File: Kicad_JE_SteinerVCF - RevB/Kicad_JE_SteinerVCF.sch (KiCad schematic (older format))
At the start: 49 parts, among them J101 HP, J102 BP, J103 LP, J104 Out, J105 CV, P101 Doepfer_Power_10pin, Q101 BC559, Q102 BC549, Q103 BC549, Q104 BC549

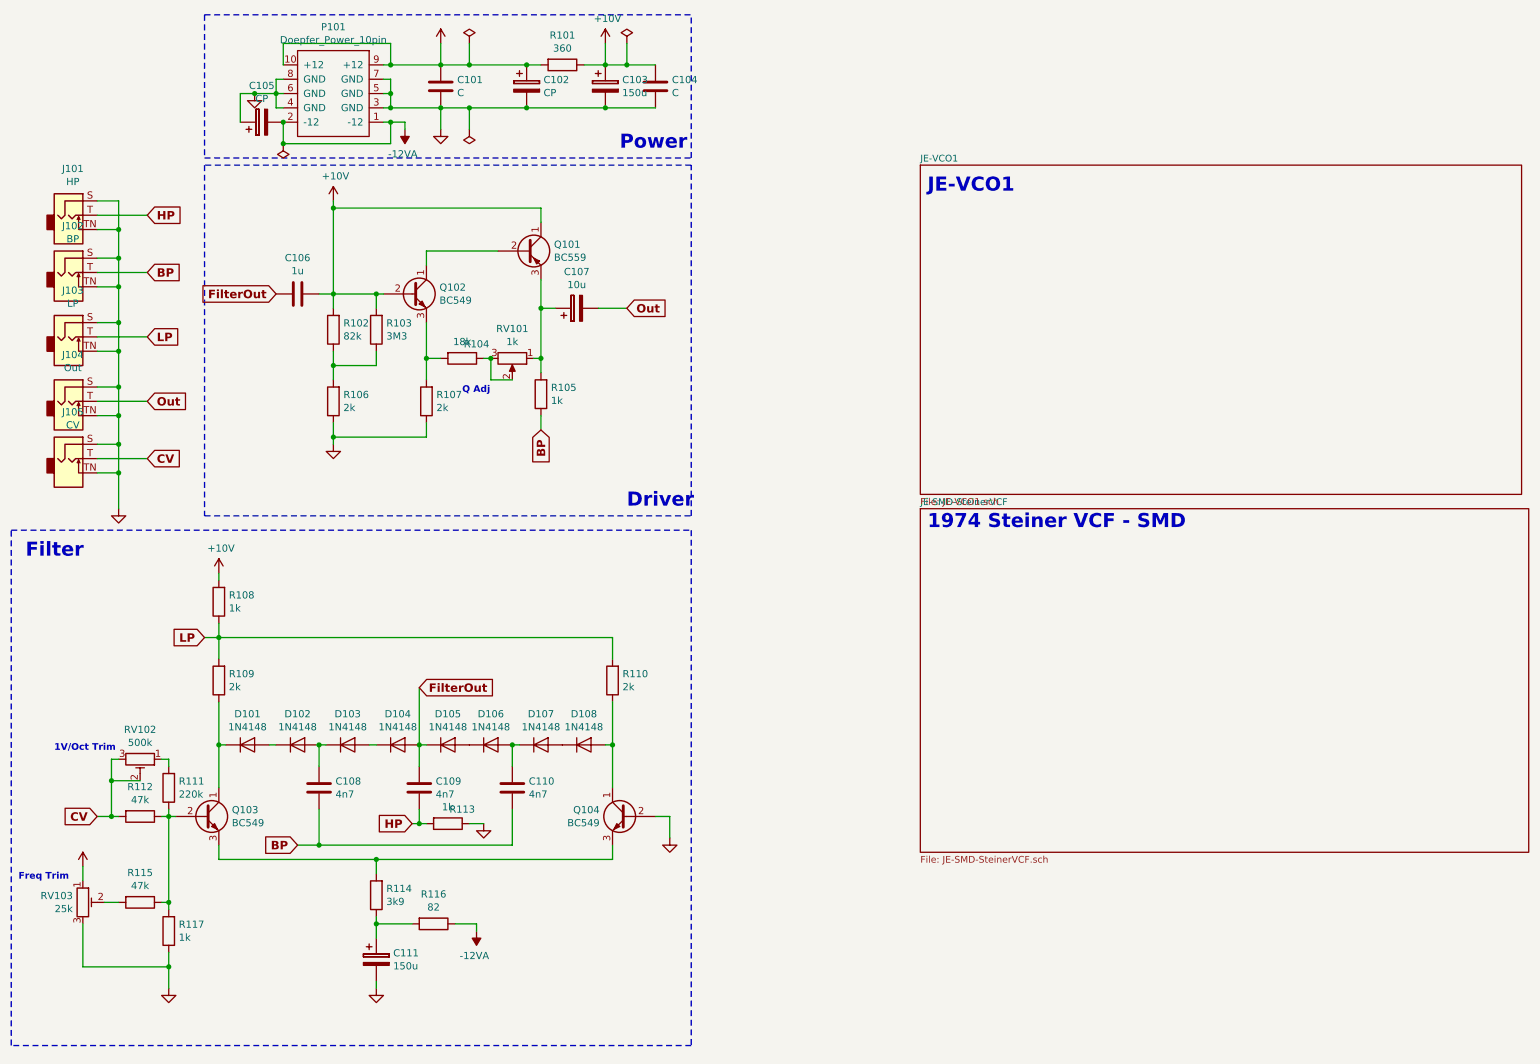
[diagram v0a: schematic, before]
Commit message: VCF Rev B THT + Extra inspiration
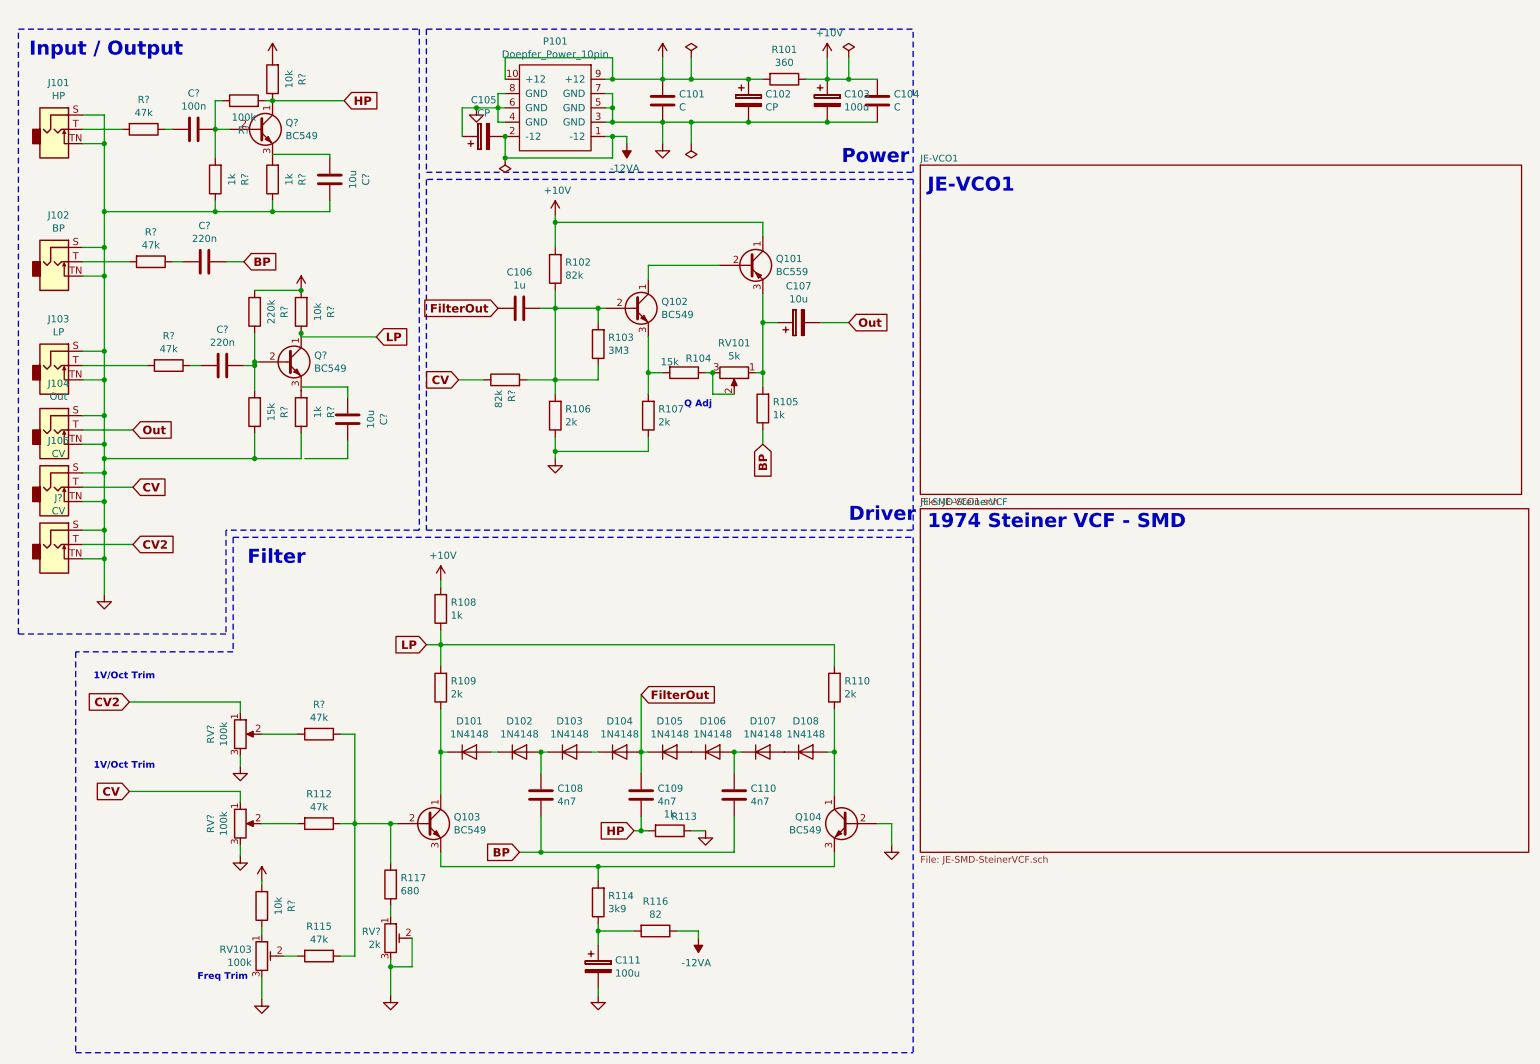
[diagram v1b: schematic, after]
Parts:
- removed R111: 220k, Resistor_THT:R_Axial_DIN0309_L9.0mm_D3.2mm_P12.70mm_Horizontal, symbol Device:R
- removed RV102: 500k, Potentiometer_THT:Potentiometer_Alps_RK09K_Single_Vertical, symbol Device:R_POT_TRIM
- added C? (x2): 220n, Capacitor_THT:C_Rect_L7.0mm_W2.0mm_P5.00mm, symbol Device:C
- added C?: 100n, Capacitor_THT:C_Rect_L7.0mm_W2.0mm_P5.00mm, symbol Device:C
- added C? (x2): 10u, Capacitor_THT:C_Rect_L7.0mm_W2.0mm_P5.00mm, symbol Device:C
- added J?: CV, AJ-Dropbox-Kicad:PJ301SM, symbol Connector:AudioJack2_SwitchT
- added Q? (x2): BC549, Package_TO_SOT_THT:TO-92_Inline, symbol Transistor_BJT:BC549
- added R?: 82k, Resistor_THT:R_Axial_DIN0309_L9.0mm_D3.2mm_P12.70mm_Horizontal, symbol Device:R
- added R? (x3): 10k, Resistor_THT:R_Axial_DIN0309_L9.0mm_D3.2mm_P12.70mm_Horizontal, symbol Device:R
- added R? (x4): 47k, Resistor_THT:R_Axial_DIN0309_L9.0mm_D3.2mm_P12.70mm_Horizontal, symbol Device:R
- added R? (x3): 1k, Resistor_THT:R_Axial_DIN0309_L9.0mm_D3.2mm_P12.70mm_Horizontal, symbol Device:R
- added R?: 220k, Resistor_THT:R_Axial_DIN0309_L9.0mm_D3.2mm_P12.70mm_Horizontal, symbol Device:R
- added R?: 15k, Resistor_THT:R_Axial_DIN0309_L9.0mm_D3.2mm_P12.70mm_Horizontal, symbol Device:R
- added R?: 100k, Resistor_THT:R_Axial_DIN0309_L9.0mm_D3.2mm_P12.70mm_Horizontal, symbol Device:R
- added RV?: 2k, Potentiometer_THT:Potentiometer_Piher_PT-6-V_Vertical, symbol Device:R_POT_TRIM
- added RV? (x2): 100k, Potentiometer_THT:Potentiometer_Alps_RK09K_Single_Vertical, symbol Device:R_POT
- C103, C111: value 150u -> 100u
- R104: value 18k -> 15k
- R117: value 1k -> 680
- RV101: value 1k -> 5k
- RV103: value 25k -> 100k
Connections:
- net +10V: no longer C106.1, Q102.2 (B), R103.2
- net +12VA: now also R?.2, R?.2, R?.2, R?.2; no longer RV103.1
- net BP: now also C?.1; no longer J102.T
- net CV: now also R?.1, RV?.1; no longer R112.2
- net GNDA: now also C?.1, J?.S, J?.TN, R?.1, R?.1, R?.1, R?.1, RV?.2, RV?.3, RV?.3, RV?.3; no longer R117.1
- net HP: now also Q?.1 (C), R?.1, R?.2; no longer J101.T
- net LP: now also Q?.1 (C), R?.1; no longer J103.T
- net at Q103.2 (B), R112.1, R115.1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: now also R?.1
- net at R102.1, R103.1, R106.2: now also C106.1, Q102.2 (B), R103.2, R?.2
- new net: R112.2, RV?.2
- new net: R117.1, RV?.1
- new net: J101.T, R?.2
- new net: J102.T, R?.2
- new net: J103.T, R?.2
- new net: R?.1, RV103.1
- new net: R?.2, RV?.2
- new net: C?.1, Q?.2 (B), R?.1, R?.2 (x2)
- new net: Q?.3 (E), R?.2 (x2)
- new net: C?.2, R?.1 (x3)
- new net CV2: J?.T, RV?.1
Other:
- note added: "Input / Output"
- moved on the sheet: C101, C102, C103, C104, C105, C106, C107, C108, C109, C110, C111, D101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

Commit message: fix reintroduced
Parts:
- added R? (x2): 1k, Resistor_THT:R_Axial_DIN0309_L9.0mm_D3.2mm_P12.70mm_Horizontal, symbol Device:R
- R?: value 1k -> 10k
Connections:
- net HP: now also R?.2; no longer Q?.1 (C), R?.1, R?.2
- net LP: now also R?.2; no longer Q?.1 (C), R?.1
- net at R102.1, R103.1, R106.2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: no longer C106.1, Q102.2 (B), R103.2
- new net: C106.1, Q102.2 (B), R103.2
- new net: Q?.1 (C), R?.1, R?.1, R?.2
- new net: Q?.1 (C), R?.1, R?.1
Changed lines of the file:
@@
 JE-VCO1
 Wire Wire Line
-	4350 2425 4350 2550
-Wire Wire Line
 	4250 2550 4350 2550
-Wire Wire Line
-	4350 2550 4350 3050
 Text GLabel 3675 3050 0    59   Input ~ 12
 CV
@@
 Wire Wire Line
 	3675 3050 3850 3050
-Connection ~ 4350 2550
 Wire Wire Line
 	4350 2550 4650 2550
@@
 Connection ~ 2375 1875
 Wire Wire Line
-	2375 1100 2875 1100
-Wire Wire Line
-	2575 2750 3100 2750
+	2375 1100 2500 1100
+Wire Wire Line
+	2575 2750 2700 2750
 Connection ~ 3200 6150
 Wire Wire Line
@@
 P 1975 1650
 F 0 "R?" V 1768 1650 50  0000 C CNN
-F 1 "1k" V 1859 1650 50  0000 C CNN
+F 1 "10k" V 1859 1650 50  0000 C CNN
 F 2 "Resistor_THT:R_Axial_DIN0309_L9.0mm_D3.2mm_P12.70mm_Horizontal" V 1905 1650 50  0001 C CNN
 F 3 "~" H 1975 1650 50  0001 C CNN
@@
 Wire Wire Line
 	1975 1500 1975 1300
+$Comp
+L Device:R R?
+U 1 1 5CAAB3D3
+P 2850 2750
+F 0 "R?" V 2643 2750 50  0000 C CNN
+F 1 "1k" V 2734 2750 50  0000 C CNN
+F 2 "Resistor_THT:R_Axial_DIN0309_L9.0mm_D3.2mm_P12.70mm_Horizontal" V 2780 2750 50  0001 C CNN
+F 3 "~" H 2850 2750 50  0001 C CNN
+	1    2850 2750
+	0    -1   -1   0
+$EndComp
+Wire Wire Line
+	3000 2750 3100 2750
+$Comp
+L Device:R R?
+U 1 1 5CAAB50A
+P 2650 1100
+F 0 "R?" V 2443 1100 50  0000 C CNN
+F 1 "1k" V 2534 1100 50  0000 C CNN
+F 2 "Resistor_THT:R_Axial_DIN0309_L9.0mm_D3.2mm_P12.70mm_Horizontal" V 2580 1100 50  0001 C CNN
+F 3 "~" H 2650 1100 50  0001 C CNN
+	1    2650 1100
+	0    -1   -1   0
+$EndComp
+Wire Wire Line
+	2800 1100 2875 1100
+Wire Wire Line
+	4350 2425 4350 3050
 $EndSCHEMATC

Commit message: mod fix
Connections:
- net CV: now also Q103.2 (B), R112.1, R115.1, R117.2, R?.1; no longer J105.T, RV?.1
- net CV2: now also J105.T; no longer J?.T
- net at C106.1, Q102.2 (B), R103.2: now also R?.2
- net at R102.1, R103.1, R106.2: no longer R?.2
- new net CV1: J?.T, RV?.1
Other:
- moved on the sheet: R?
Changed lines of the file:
@@
 $EndComp
 Text GLabel 1375 5925 0    59   Input ~ 12
-CV
+CV1
 $Comp
 L Device:R R117
@@
 	1200 3500 1200 3600
 Text GLabel 1400 3800 2    59   Input ~ 12
-CV
+CV2
 Text GLabel 1400 3400 2    59   Input ~ 12
 Out
@@
 JE-VCO1
 Wire Wire Line
-	4250 2550 4350 2550
-Text GLabel 3675 3050 0    59   Input ~ 12
+	4250 2550 4300 2550
+Text GLabel 3750 2750 0    59   Input ~ 12
 CV
 $Comp
 L Device:R R?
 U 1 1 5C6D5FD8
-P 4000 3050
-F 0 "R?" H 3930 3004 50  0000 R CNN
-F 1 "82k" H 3930 3095 50  0000 R CNN
-F 2 "Resistor_THT:R_Axial_DIN0309_L9.0mm_D3.2mm_P12.70mm_Horizontal" V 3930 3050 50  0001 C CNN
-F 3 "~" H 4000 3050 50  0001 C CNN
-	1    4000 3050
+P 4075 2750
+F 0 "R?" H 4005 2704 50  0000 R CNN
+F 1 "82k" H 4005 2795 50  0000 R CNN
+F 2 "Resistor_THT:R_Axial_DIN0309_L9.0mm_D3.2mm_P12.70mm_Horizontal" V 4005 2750 50  0001 C CNN
+F 3 "~" H 4075 2750 50  0001 C CNN
+	1    4075 2750
 	0    -1   -1   0
 $EndComp
 Wire Wire Line
-	4150 3050 4350 3050
-Wire Wire Line
-	3675 3050 3850 3050
+	3750 2750 3925 2750
 Wire Wire Line
 	4350 2550 4650 2550
@@
 	1200 4300 1200 4550
 Text GLabel 1400 4200 2    59   Input ~ 12
-CV2
+CV1
 Wire Wire Line
 	1050 4200 1400 4200
@@
 Wire Wire Line
 	4350 2425 4350 3050
+Wire Wire Line
+	4225 2750 4300 2750
+Wire Wire Line
+	4300 2750 4300 2550
+Connection ~ 4300 2550
+Wire Wire Line
+	4300 2550 4350 2550
+Text GLabel 3200 5975 1    59   Input ~ 12
+CV
+Wire Wire Line
+	3200 5975 3200 6150
 $EndSCHEMATC

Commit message: DRC RevB
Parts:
- gave numbers to parts that had none: 27
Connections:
- net GNDA: now also C116.1
- net at Q105.3 (E), R122.2: now also C113.2
- net at Q106.3 (E), R130.2: now also C116.2
